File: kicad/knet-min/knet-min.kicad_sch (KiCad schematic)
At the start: 24 parts, among them J1 Conn_01x02_Socket, J3 Conn_01x04, J4 Conn_01x02, J5 Conn_01x02_Socket, SW1 SW_SPST, U1 MC3487N, U11 Mainboard, U2 MC3486N, U3 74LS06, U4 74LS157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

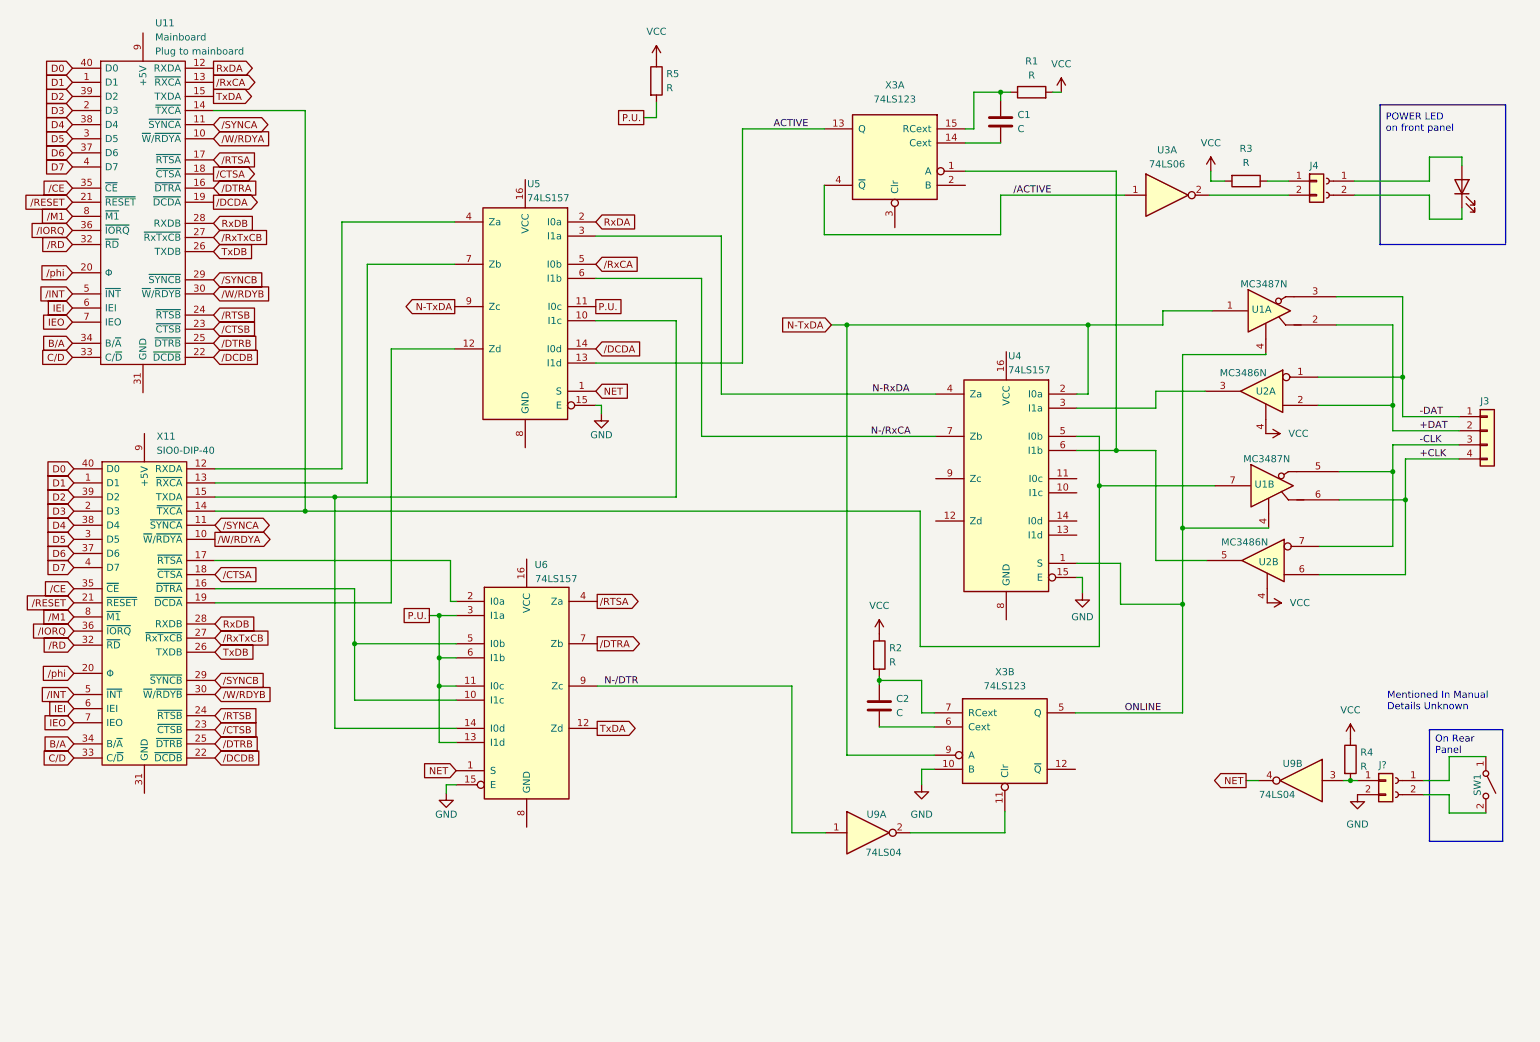
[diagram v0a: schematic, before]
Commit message: add minimal KayNet schematic
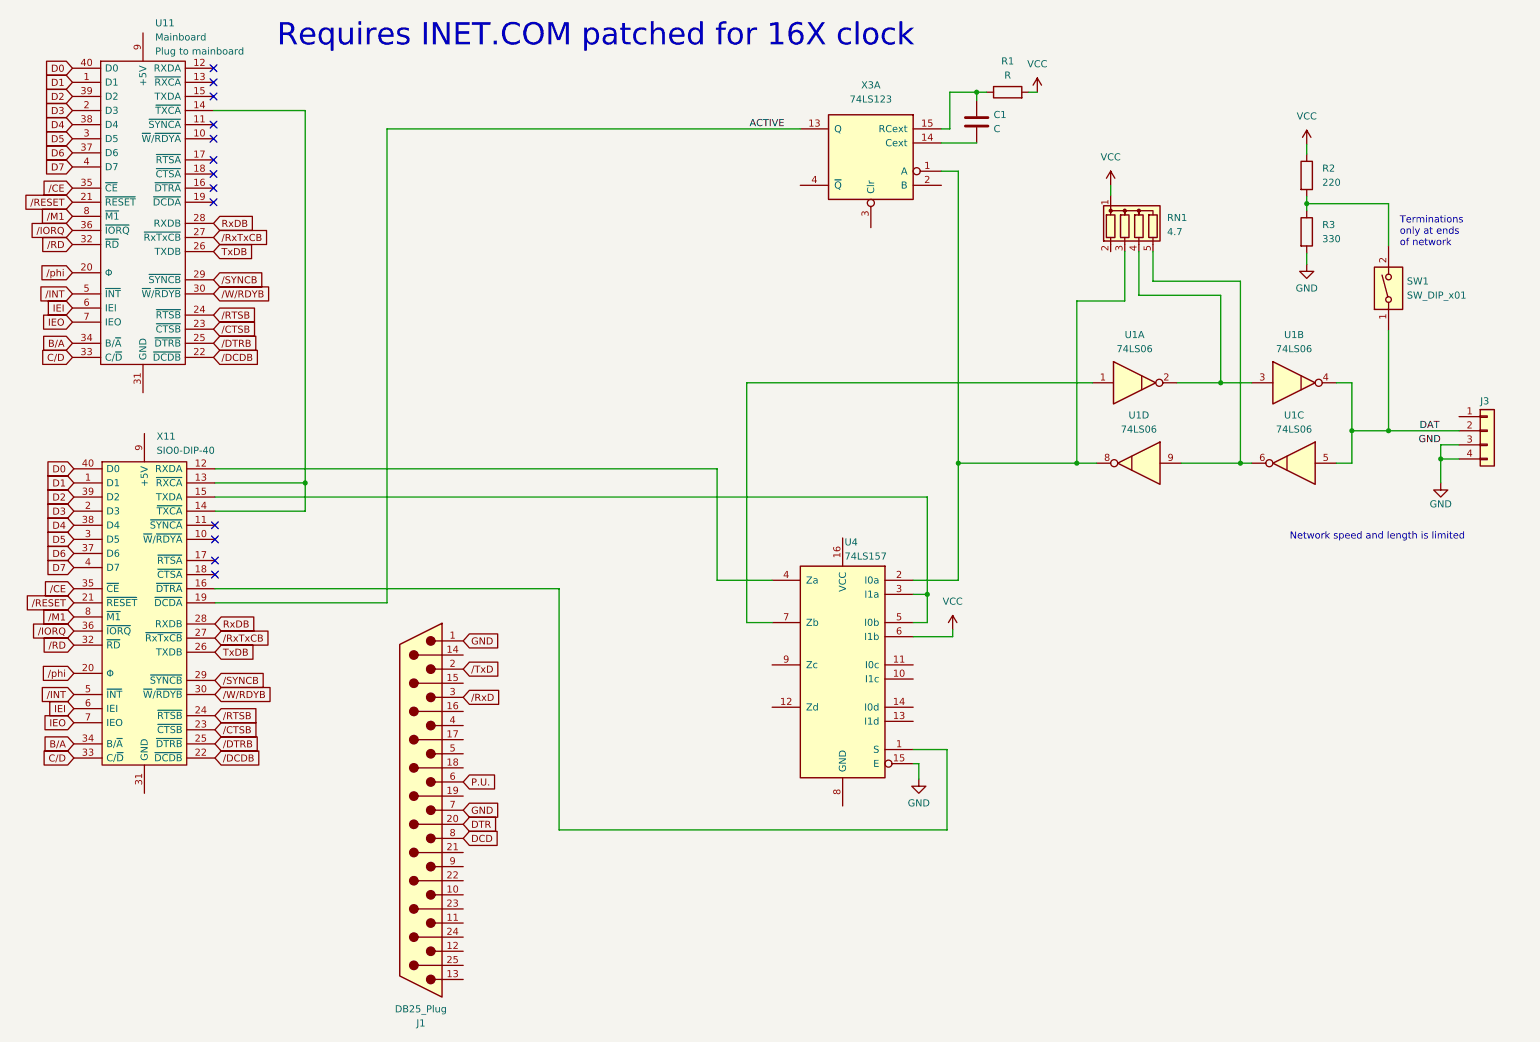
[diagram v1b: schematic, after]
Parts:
- removed C2: C, symbol Device:C
- removed D1: LED, symbol Device:LED
- removed J1, J5: Conn_01x02_Socket, symbol Connector:Conn_01x02_Socket
- removed J4, J?: Conn_01x02, symbol Connector_Generic:Conn_01x02
- removed R4, R5: R, symbol Device:R
- removed SW1: SW_SPST, symbol Switch:SW_SPST
- removed U1: MC3487N, Package_DIP:DIP-16_W7.62mm, symbol Interface_LineDriver:MC3487N
- removed U2: MC3486N, Package_DIP:DIP-14_W7.62mm, symbol Interface_LineDriver:MC3486N
- removed U3: 74LS06, symbol 74xx:74LS06
- removed U5, U6: 74LS157, symbol 74xx:74LS157
- removed U9: 74LS04, symbol 74xx:74LS04
- removed unit 2 of X3
- added J1: DB25_Plug, symbol Connector:DB25_Plug
- added RN1: 4.7, Resistor_THT:R_Array_SIP5, symbol Device:R_Network04
- added SW1: SW_DIP_x01, symbol Switch:SW_DIP_x01
- added U1: 74LS06, symbol 74xx:74LS06
- R2: value R -> 220
- R3: value R -> 330
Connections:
- net +CLK is gone; now on net GND: J3.4 (Pin_4)
- net -CLK is gone; now on net GND: J3.3 (Pin_3)
- net N-RxDA is gone; now on an unnamed net: U4.4 (Za)
- net N-TxDA is gone; now on an unnamed net: U4.2 (I0a)
- net ONLINE is gone; now on an unnamed net: U4.1 (S)
- net ACTIVE: now also X11.19 (~{DCDA})
- net GND: now also R3.2, J1.1, J1.7
- net P.U.: now also J1.6
- net VCC: now also U4.6 (I1b), RN1.1 (common); no longer R3.2
- net at U4.3 (I1a): now also U4.5 (I0b), X11.15 (TXDA)
- net at U11.14 (~{TXCA}), X11.14 (~{TXCA}): now also X11.13 (~{RXCA}); no longer U4.5 (I0b)
- net at X3.1 (A): now also RN1.3 (R2), U1.8; no longer U4.6 (I1b)
- net at R2.2: now also R3.1, SW1.2
- net +DAT renamed DAT
- net DAT: now also SW1.1, U1.4, U1.5
- net -DAT: no longer names the net of J3.1 (Pin_1)
- net N-/RxCA: no longer names the net of U4.7 (Zb)
- net N-/RxCA: now also U1.1
- net RxDA: no longer names the net of U11.12 (RXDA)
- net TxDA: no longer names the net of U11.15 (TXDA)
- net /ACTIVE: no longer names the net of X3.4 (~{Q})
- net /CTSA: no longer names the net of X11.18 (~{CTSA})
- net /CTSA: no longer U11.18 (~{CTSA})
- net /DCDA: no longer names the net of U11.19 (~{DCDA})
- net /DTRA: no longer names the net of U11.16 (~{DTRA})
- net /RTSA: no longer names the net of U11.17 (~{RTSA})
- net /RxCA: no longer names the net of U11.13 (~{RXCA})
- net /SYNCA: no longer names the net of X11.11 (~{SYNCA})
- net /SYNCA: no longer U11.11 (~{SYNCA})
- net /W/RDYA: no longer names the net of X11.10 (~{W}/~{RDYA})
- net /W/RDYA: no longer U11.10 (~{W}/~{RDYA})
- new net: RN1.4 (R3), U1.2, U1.3
- new net: RN1.5 (R4), U1.6, U1.9
- new net DCD: J1.8
- new net DTR: J1.20 (P20)
- new net /RxD: J1.3
- new net /TxD: J1.2
- no-connect marks 0 -> 13
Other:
- note added: "Network speed and length is limited"
- note added: "Requires INET.COM patched for 16X clock"
- note added: "Terminations only at ends of network"
- note removed: "Mentioned In Manual Details Unknown"
- note removed: "On Rear Panel"
- note removed: "POWER LED on front panel"
- title: Possible KayNet-ULCNet equivalent -> KayNet-ULCNet minimum circuit
- moved on the sheet: C1, R1, U4, X3A
